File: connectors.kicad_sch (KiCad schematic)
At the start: 26 parts, among them J2 USB_C_Receptacle_USB2.0_14P, J3 Conn_01x02, M1 Motor_Servo, M2 Motor_Servo, Q1 Q_NMOS, Q2 Q_NMOS, U5 LM74502

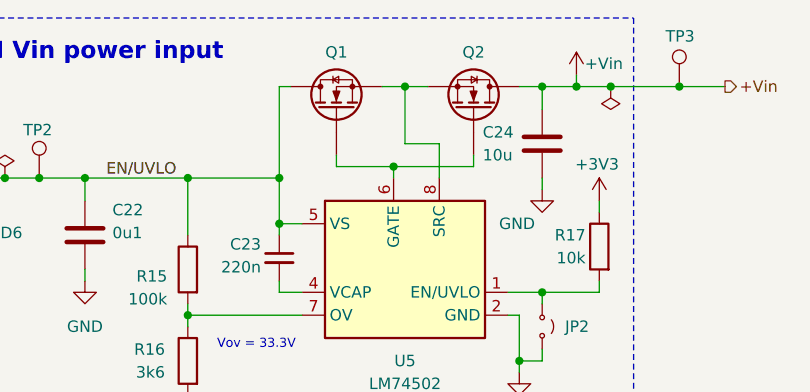
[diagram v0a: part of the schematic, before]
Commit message: schem: update MOSFETs symbol
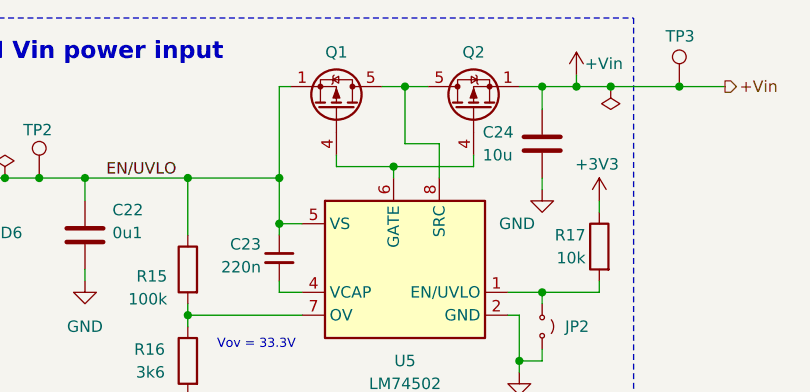
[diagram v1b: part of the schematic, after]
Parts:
- Q1, Q2: symbol Device:Q_NMOS -> Transistor_FET:SiS415DNT
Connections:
- net +Vin: now also Q2.1 (S), Q2.2 (S), Q2.3 (S); no longer Q2.D
- net EN/UVLO: now also Q1.1 (S), Q1.2 (S), Q1.3 (S); no longer Q1.D
- new net: Q1.4 (G), Q2.4 (G), U5.6 (GATE)
- new net: Q1.5 (D), Q2.5 (D), U5.8 (SRC)
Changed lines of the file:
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@@
 	)
 	(symbol
-		(lib_id "Device:Q_NMOS")
-		(at 217.17 87.63 270)
-		(mirror x)
+		(lib_id "Transistor_FET:SiS415DNT")
+		(at 217.17 87.63 90)
 		(unit 1)
 		(exclude_from_sim no)
@@
 		)
 		(property "Footprint" "Package_SO:Vishay_PowerPAK_1212-8_Single"
-			(at 219.71 82.55 0)
+			(at 214.63 82.55 0)
 			(effects
 				(font
@@
 			)
 		)
-		(pin "S"
-		)
-		(pin "G"
-		)
-		(pin "D"
+		(pin "5"
+		)
+		(pin "1"
+		)
+		(pin "4"
+		)
+		(pin "2"
+		)
+		(pin "3"
 		)
 		(instances
@@
 	)
 	(symbol
-		(lib_id "Device:Q_NMOS")
-		(at 201.93 87.63 90)
-		(unit 1)
-		(exclude_from_sim no)
-		(in_bom yes)
-		(on_board yes)
-		(dnp no)
-		(fields_autoplaced yes)
+		(lib_id "Transistor_FET:SiS415DNT")
+		(at 201.93 87.63 270)
+		(mirror x)
+		(unit 1)
+		(exclude_from_sim no)
+		(in_bom yes)
+		(on_board yes)
+		(dnp no)
 		(property "Reference" "Q1"
 			(at 201.93 81.28 90)
@@
 		)
 		(property "Footprint" "Package_SO:Vishay_PowerPAK_1212-8_Single"
-			(at 199.39 82.55 0)
+			(at 204.47 82.55 0)
 			(effects
 				(font
@@
 			)
 		)
-		(pin "S"
-		)
-		(pin "G"
-		)
-		(pin "D"
-		)
-		(instances
+		(pin "2"
+		)
+		(pin "5"
+		)
+		(pin "1"
+		)
+		(pin "3"
+		)
+		(pin "4"
+		)
+		(instances

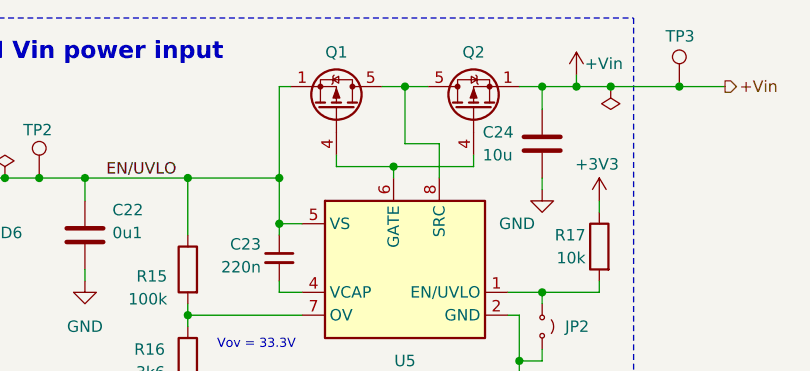
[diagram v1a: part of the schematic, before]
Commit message: schem: update MOSFETs footprints to correct N-channel
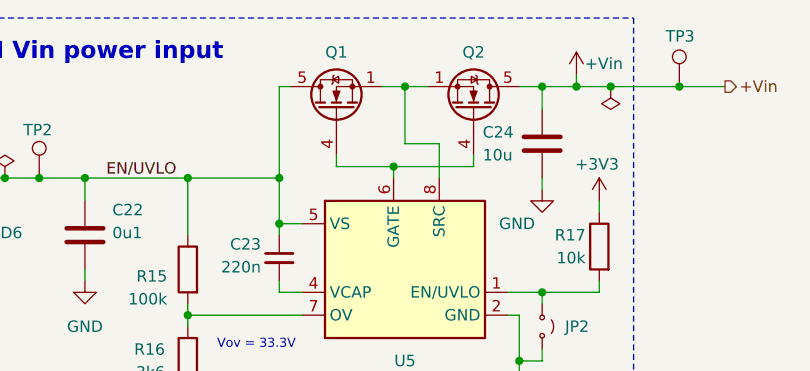
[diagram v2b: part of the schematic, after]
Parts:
- Q1, Q2: symbol Transistor_FET:SiS415DNT -> Transistor_FET:SiS454DN
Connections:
- net +Vin: now also Q2.5 (D); no longer Q2.1 (S), Q2.2 (S), Q2.3 (S)
- net EN/UVLO: now also Q1.5 (D); no longer Q1.1 (S), Q1.2 (S), Q1.3 (S)
- new net: Q1.1 (S), Q1.2 (S), Q1.3 (S), Q2.1 (S), Q2.2 (S), Q2.3 (S), U5.8 (SRC)
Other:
- moved on the sheet: Q1, Q2
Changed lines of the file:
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@@
 	)
 	(symbol
-		(lib_id "Transistor_FET:SiS415DNT")
-		(at 217.17 87.63 90)
+		(lib_id "Transistor_FET:SiS454DN")
+		(at 217.17 87.63 270)
+		(mirror x)
 		(unit 1)
 		(exclude_from_sim no)
@@
 		)
 		(property "Footprint" "Package_SO:Vishay_PowerPAK_1212-8_Single"
-			(at 214.63 82.55 0)
+			(at 219.71 82.55 0)
 			(effects
 				(font
@@
 	)
 	(symbol
-		(lib_id "Transistor_FET:SiS415DNT")
-		(at 201.93 87.63 270)
-		(mirror x)
+		(lib_id "Transistor_FET:SiS454DN")
+		(at 201.93 87.63 90)
 		(unit 1)
 		(exclude_from_sim no)
@@
 		)
 		(property "Footprint" "Package_SO:Vishay_PowerPAK_1212-8_Single"
-			(at 204.47 82.55 0)
-			(effects
-				(font
+			(at 199.39 82.55 0)
+			(effects
+				(font

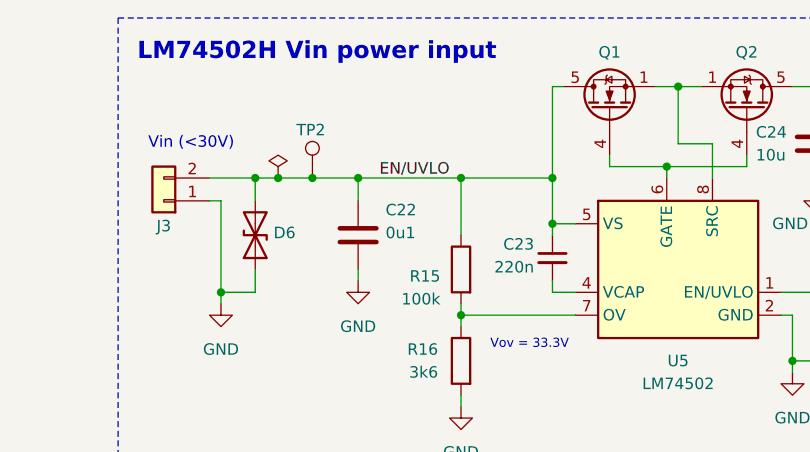
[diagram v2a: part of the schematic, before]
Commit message: schem: remove unnecesary label
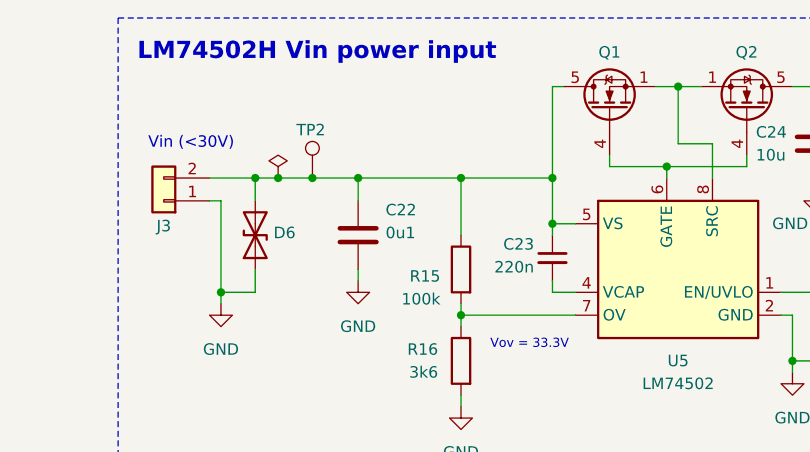
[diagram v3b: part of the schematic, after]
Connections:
- net EN/UVLO: no longer names the net of C22.1, C23.1, D6.2 (A2), J3.2 (Pin_2), Q1.5 (D), R15.1, TP2.1, U5.5 (VS)
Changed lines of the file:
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@@
-		)
-	)
-	(label "EN/UVLO"
-		(at 184.15 95.25 180)
-		(effects
-			(font
-				(size 1.27 1.27)
-			)
-			(justify right bottom)
 		)
 	)

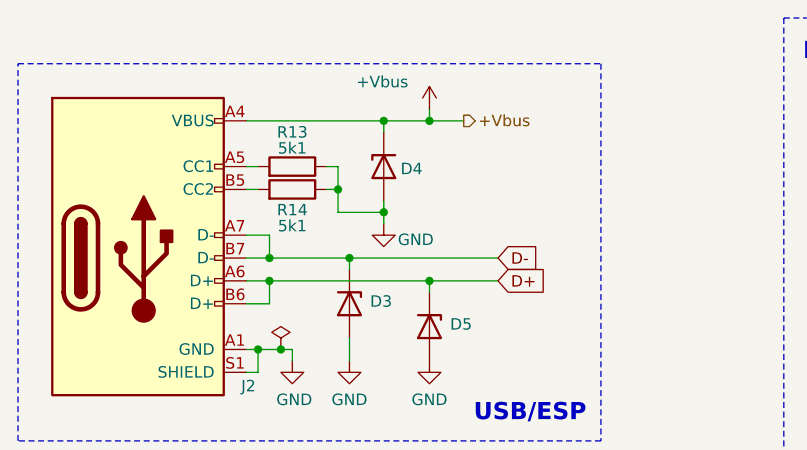
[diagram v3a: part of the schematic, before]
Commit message: schem: fix BOM
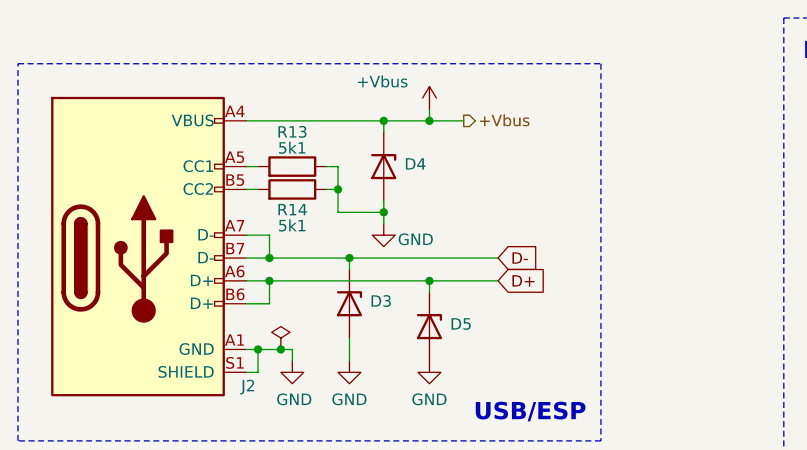
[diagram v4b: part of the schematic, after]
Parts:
- D4: value P6SMB6.8CA/TR13 -> H5VU10U; Basic Y -> E; JLCPCB Part # C78395 -> C22395519; Manufacturer Brightking -> hongjiacheng; Manufacturer Part Number P6SMB6.8CA/TR13 -> H5VU10U
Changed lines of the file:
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@@
-	)
-	(symbol
-		(lib_id "GLCS:H5VU10U")
-		(at 102.87 93.98 90)
-		(mirror x)
-		(unit 1)
-		(exclude_from_sim no)
-		(in_bom yes)
-		(on_board yes)
-		(dnp no)
-		(property "Reference" "D4"
-			(at 107.188 94.234 90)
-			(effects
-				(font
-					(size 1.27 1.27)
-				)
-				(justify left)
-			)
-		)
-		(property "Value" "P6SMB6.8CA/TR13"
-			(at 100.33 95.2499 90)
-			(effects
-				(font
-					(size 1.27 1.27)
-				)
-				(justify left)
-				(hide yes)
-			)
-		)
-		(property "Footprint" "GLCS:Diode_DFN1006"
-			(at 107.315 93.98 0)
-			(effects
-				(font
-					(size 1.27 1.27)
-				)
-				(hide yes)
-			)
-		)
-		(property "Datasheet" "https://datasheet.lcsc.com/lcsc/2504101957_hongjiacheng-H5VU10U_C22395519.pdf"
-			(at 102.87 93.98 0)
-			(effects
-				(font
-					(size 1.27 1.27)
-				)
-				(hide yes)
-			)
-		)
-		(property "Description" "-55℃~+155℃ 0.8pF 16V 200nA 55W@8/20us 5A@8/20us 5V 6V ESD IEC 61000-4-2 Unidirectional DFN1006-2L ESD and Surge Protection (TVS/ESD) ROHS"
-			(at 102.87 93.98 0)
-			(effects
-				(font
-					(size 1.27 1.27)
-				)
-				(hide yes)
-			)
-		)
-		(property "Basic" "Y"
-			(at 102.87 93.98 90)
-			(effects
-				(font
-					(size 1.27 1.27)
-				)
-				(hide yes)
-			)
-		)
-		(property "JLCPCB Part #" "C78395"
-			(at 102.87 93.98 90)
-			(effects
-				(font
-					(size 1.27 1.27)
-				)
-				(hide yes)
-			)
-		)
-		(property "Manufacturer" "Brightking"
-			(at 102.87 93.98 90)
-			(effects
-				(font
-					(size 1.27 1.27)
-				)
-				(hide yes)
-			)
-		)
-		(property "Manufacturer Part Number" "P6SMB6.8CA/TR13"
-			(at 102.87 93.98 90)
-			(effects
-				(font
-					(size 1.27 1.27)
-				)
-				(hide yes)
-			)
-		)
-		(pin "1"
-		)
-		(pin "2"
-		)
-		(instances
-			(project "motor-power-poc"
-				(path "/a1dc4c9e-7b20-4b66-a693-9133bc644c6b/dba74ea3-505d-49e4-ba26-48f567962081"
-					(reference "D4")
-					(unit 1)
-				)
-			)
-		)
 	)
 	(symbol
@@
 					(unit 1)
 				)
+			)
+		)
+	)
+	(symbol
+		(lib_id "GLCS:H5VU10U")
+		(at 102.87 93.98 270)
+		(unit 1)
+		(exclude_from_sim no)
+		(in_bom yes)
+		(on_board yes)
+		(dnp no)
+		(property "Reference" "D4"
+			(at 105.156 93.726 90)
+			(effects
+				(font
+					(size 1.27 1.27)
+				)
+				(justify left)
+			)
+		)
+		(property "Value" "H5VU10U"
+			(at 105.41 95.2499 90)
+			(effects
+				(font
+					(size 1.27 1.27)
+				)
+				(justify left)
+				(hide yes)
+			)
+		)
+		(property "Footprint" "GLCS:Diode_DFN1006"
+			(at 98.425 93.98 0)
+			(effects
+				(font
+					(size 1.27 1.27)
+				)
+				(hide yes)
+			)
+		)
+		(property "Datasheet" "https://datasheet.lcsc.com/lcsc/2504101957_hongjiacheng-H5VU10U_C22395519.pdf"
+			(at 102.87 93.98 0)
+			(effects
+				(font
+					(size 1.27 1.27)
+				)
+				(hide yes)
+			)
+		)
+		(property "Description" "-55℃~+155℃ 0.8pF 16V 200nA 55W@8/20us 5A@8/20us 5V 6V ESD IEC 61000-4-2 Unidirectional DFN1006-2L ESD and Surge Protection (TVS/ESD) ROHS"
+			(at 102.87 93.98 0)
+			(effects
+				(font
+					(size 1.27 1.27)
+				)
+				(hide yes)
+			)
+		)
+		(property "Basic" "E"
+			(at 102.87 93.98 90)
+			(effects
+				(font
+					(size 1.27 1.27)
+				)
+				(hide yes)
+			)
+		)
+		(property "JLCPCB Part #" "C22395519"
+			(at 102.87 93.98 90)
+			(effects
+				(font
+					(size 1.27 1.27)
+				)
+				(hide yes)
+			)
+		)
+		(property "Manufacturer" "hongjiacheng"
+			(at 102.87 93.98 90)
+			(effects
+				(font
+					(size 1.27 1.27)
+				)
+				(hide yes)
+			)
+		)
+		(property "Manufacturer Part Number" "H5VU10U"
+			(at 102.87 93.98 90)
+			(effects
+				(font
+					(size 1.27 1.27)
+				)
+				(hide yes)
+			)
+		)
+		(pin "1"
+		)
+		(pin "2"
+		)
+		(instances
+			(project "motor-power-poc"
+				(path "/a1dc4c9e-7b20-4b66-a693-9133bc644c6b/dba74ea3-505d-49e4-ba26-48f567962081"
+					(reference "D4")
+					(unit 1)
+				)
